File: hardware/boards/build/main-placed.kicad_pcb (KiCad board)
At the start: 4 copper layers, 177.9 x 107.5 mm, 146 parts

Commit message: Fix hardware pipeline: SD card position, faceplate holes, 3D assembly stack-up
- Fix SD card slot placement below PLAY button with component-map fallback
- Rebuild PJS008U 3D model as hollow card cage, align with faceplate cutout
- Inset USB-C connector flush with main board edge
- Add clock jack holes, SD cutout, JetBrains Mono fonts to faceplate
- Correct 3D assembly Z spacing from actual PJ398SM model measurements
- Improve explode animation: anchor control board, smoother slider
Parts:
- REF**: moved to F.Cu
- moved REF** 136.9 mm to (172.9, 53.8), turned to 90 degrees
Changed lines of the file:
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@@
 		)
 	)
+	(footprint "USB_C_Receptacle:USB_C_Receptacle"
+		(layer "F.Cu")
+		(at 172.88 53.75 90)
+		(property "Reference" "REF**"
+			(at 0 -6 90)
+			(layer "F.SilkS")
+			(effects
+				(font
+					(size 1 1)
+					(thickness 0.15)
+				)
+			)
+		)
+		(property "Value" "USB_C_Receptacle"
+			(at 0 6 90)
+			(layer "F.Fab")
+			(effects
+				(font
+					(size 1 1)
+					(thickness 0.15)
+				)
+			)
+		)
+		(property "Datasheet" ""
+			(at 0 0 90)
+			(layer "F.Fab")
+			(hide yes)
+			(effects
+				(font
+					(size 1.27 1.27)
+					(thickness 0.15)
+				)
+			)
+		)
+		(property "Description" ""
+			(at 0 0 90)
+			(layer "F.Fab")
+			(hide yes)
+			(effects
+				(font
+					(size 1.27 1.27)
+					(thickness 0.15)
+				)
+			)
+		)
+		(property "LCSC" "C165948"
+			(at 0 0 90)
+			(layer "User.9")
+			(hide yes)
+			(effects
+				(font
+					(size 1 1)
+					(thickness 0.15)
+				)
+			)
+		)
+		(property "Manufacturer" "Korean Hroparts Elec"
+			(at 0 0 90)
+			(layer "User.9")
+			(hide yes)
+			(effects
+				(font
+					(size 1 1)
+					(thickness 0.15)
+				)
+			)
+		)
+		(property "Partnumber" "TYPE-C-31-M-12"
+			(at 0 0 90)
+			(layer "User.9")
+			(hide yes)
+			(effects
+				(font
+					(size 1 1)
+					(thickness 0.15)
+				)
+			)
+		)
+		(property "atopile_address" "usb"
+			(at 0 0 90)
+			(layer "User.9")
+			(hide yes)
+			(effects
+				(font
+					(size 1 1)
+					(thickness 0.15)
+				)
+			)
+		)
+		(property "lcsc_id" "C165948"
+			(at 0 0 90)
+			(layer "User.9")
+			(hide yes)
+			(effects
+				(font
+					(size 1 1)
+					(thickness 0.15)
+				)
+			)
+		)
+		(attr smd)
+		(pad "" smd rect
+			(at -4.32 -1.45 90)
+			(size 1 2.1)
+			(layers "F.Cu" "F.Mask" "F.Paste")
+		)
+		(pad "1" smd rect
+			(at -3.2 -3.2 90)
+			(size 0.6 1.2)
+			(layers "F.Cu" "F.Mask" "F.Paste")
+			(net 34 "hv")
+		)
+		(pad "2" smd rect
+			(at -2.4 -3.2 90)
+			(size 0.6 1.2)
+			(layers "F.Cu" "F.Mask" "F.Paste")
+			(net 34 "hv")
+		)
+		(pad "3" smd rect
+			(at -0.8 -3.2 90)
+			(size 0.6 1.2)
+			(layers "F.Cu" "F.Mask" "F.Paste")
+			(net 142 "3")
+		)
+		(pad "4" smd rect
+			(at 0 -3.2 90)
+			(size 0.6 1.2)
+			(layers "F.Cu" "F.Mask" "F.Paste")
+			(net 145 "DM")
+		)
+		(pad "5" smd rect
+			(at 0.8 -3.2 90)
+			(size 0.6 1.2)
+			(layers "F.Cu" "F.Mask" "F.Paste")
+			(net 144 "5")
+		)
+		(pad "6" smd rect
+			(at 2.4 -3.2 90)
+			(size 0.6 1.2)
+			(layers "F.Cu" "F.Mask" "F.Paste")
+			(net 146 "6")
+		)
+		(pad "7" smd rect
+			(at 3.2 -3.2 90)
+			(size 0.6 1.2)
+			(layers "F.Cu" "F.Mask" "F.Paste")
+			(net 34 "hv")
+		)
+		(embedded_fonts no)
+		(model "${KICAD9_3DMODEL_DIR}/Connector_USB.3dshapes/USB_C_Receptacle_GCT_USB4085.step"
+			(offset (xyz -2.975 2.43 0))
+			(scale (xyz 1 1 1))
+			(rotate (xyz 0 0 0))
+		)
+	)
 	(footprint "ShroudedHeader2x16:ShroudedHeader2x16"
 		(layer "F.Cu")
@@
 		)
 	)
-	(footprint "USB_C_Receptacle:USB_C_Receptacle"
-		(layer "B.Cu")
-		(at 36 55.01 180)
-		(property "Reference" "REF**"
-			(at 0 6 0)
-			(layer "B.SilkS")
-			(effects
-				(font
-					(size 1 1)
-					(thickness 0.15)
-				)
-				(justify mirror)
-			)
-		)
-		(property "Value" "USB_C_Receptacle"
-			(at 0 -6 0)
-			(layer "B.Fab")
-			(effects
-				(font
-					(size 1 1)
-					(thickness 0.15)
-				)
-				(justify mirror)
-			)
-		)
-		(property "Datasheet" ""
-			(at 0 0 0)
-			(layer "B.Fab")
-			(hide yes)
-			(effects
-				(font
-					(size 1.27 1.27)
-					(thickness 0.15)
-				)
-				(justify mirror)
-			)
-		)
-		(property "Description" ""
-			(at 0 0 0)
-			(layer "B.Fab")
-			(hide yes)
-			(effects
-				(font
-					(size 1.27 1.27)
-					(thickness 0.15)
-				)
-				(justify mirror)
-			)
-		)
-		(property "LCSC" "C165948"
-			(at 0 0 0)
-			(layer "User.9")
-			(hide yes)
-			(effects
-				(font
-					(size 1 1)
-					(thickness 0.15)
-				)
-			)
-		)
-		(property "Manufacturer" "Korean Hroparts Elec"
-			(at 0 0 0)
-			(layer "User.9")
-			(hide yes)
-			(effects
-				(font
-					(size 1 1)
-					(thickness 0.15)
-				)
-			)
-		)
-		(property "Partnumber" "TYPE-C-31-M-12"
-			(at 0 0 0)
-			(layer "User.9")
-			(hide yes)
-			(effects
-				(font
-					(size 1 1)
-					(thickness 0.15)
-				)
-			)
-		)
-		(property "atopile_address" "usb"
-			(at 0 0 0)
-			(layer "User.9")
-			(hide yes)
-			(effects
-				(font
-					(size 1 1)
-					(thickness 0.15)
-				)
-			)
-		)
-		(property "lcsc_id" "C165948"
-			(at 0 0 0)
-			(layer "User.9")
-			(hide yes)
-			(effects
-				(font
-					(size 1 1)
-					(thickness 0.15)
-				)
-			)
-		)
-		(attr smd)
-		(pad "" smd rect
-			(at -4.32 1.45 180)
-			(size 1 2.1)
-			(layers "B.Cu" "B.Mask" "B.Paste")
-		)
-		(pad "1" smd rect
-			(at -3.2 3.2 180)
-			(size 0.6 1.2)
-			(layers "B.Cu" "B.Mask" "B.Paste")
-			(net 34 "hv")
-		)
-		(pad "2" smd rect
-			(at -2.4 3.2 180)
-			(size 0.6 1.2)
-			(layers "B.Cu" "B.Mask" "B.Paste")
-			(net 34 "hv")
-		)
-		(pad "3" smd rect
-			(at -0.8 3.2 180)
-			(size 0.6 1.2)
-			(layers "B.Cu" "B.Mask" "B.Paste")
-			(net 142 "3")
-		)
-		(pad "4" smd rect
-			(at 0 3.2 180)
-			(size 0.6 1.2)
-			(layers "B.Cu" "B.Mask" "B.Paste")
-			(net 145 "DM")
-		)
-		(pad "5" smd rect
-			(at 0.8 3.2 180)
-			(size 0.6 1.2)
-			(layers "B.Cu" "B.Mask" "B.Paste")
-			(net 144 "5")
-		)
-		(pad "6" smd rect
-			(at 2.4 3.2 180)
-			(size 0.6 1.2)
-			(layers "B.Cu" "B.Mask" "B.Paste")
-			(net 146 "6")
-		)
-		(pad "7" smd rect
-			(at 3.2 3.2 180)
-			(size 0.6 1.2)
-			(layers "B.Cu" "B.Mask" "B.Paste")
-			(net 34 "hv")
-		)
-		(embedded_fonts no)
-		(model "${KICAD9_3DMODEL_DIR}/Connector_USB.3dshapes/USB_C_Receptacle_GCT_USB4085.step"
-			(offset (xyz -2.975 2.43 0))
-			(scale (xyz 1 1 1))
-			(rotate (xyz 0 0 0))
-		)
-	)
 	(footprint "AMS1117-3.3:SOT-223"
 		(layer "B.Cu")
@@
 	)
 	(gr_line
-		(start 0 0)
-		(end 177.88 0)
+		(start 177.88 0)
+		(end 177.88 107.5)
 		(stroke
 			(width 0.1)
@@
 	)
 	(gr_line
-		(start 0 107.5)
-		(end 0 0)
+		(start 0 0)
+		(end 177.88 0)
 		(stroke
 			(width 0.1)
@@
 	)
 	(gr_line
-		(start 177.88 107.5)
-		(end 0 107.5)
+		(start 0 107.5)
+		(end 0 0)
 		(stroke
 			(width 0.1)
@@
 	)
 	(gr_line
-		(start 177.88 0)
-		(end 177.88 107.5)
+		(start 177.88 107.5)
+		(end 0 107.5)
 		(stroke
 			(width 0.1)

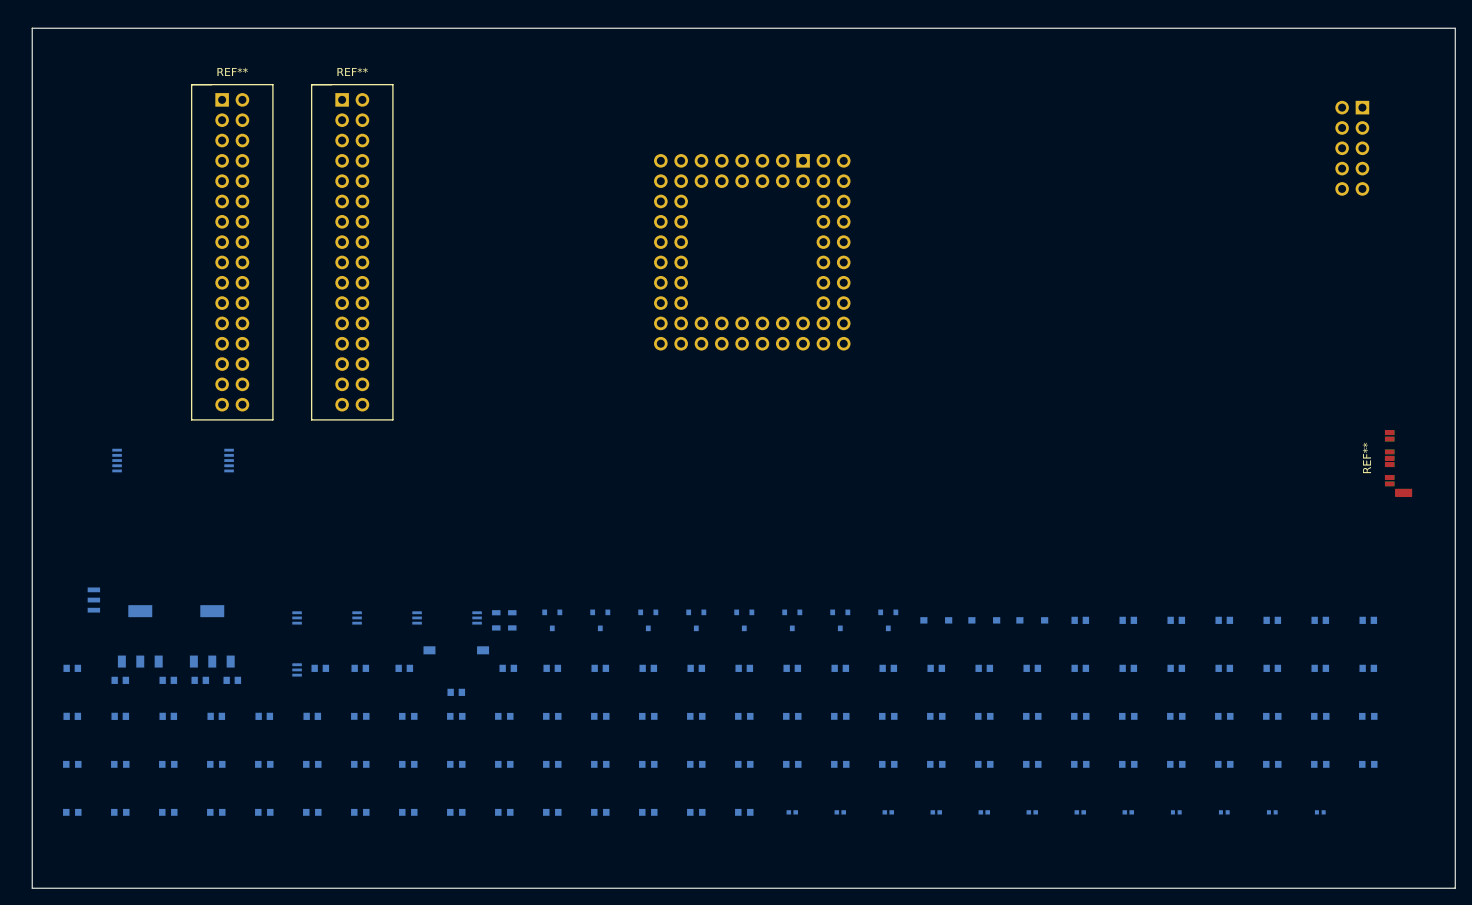
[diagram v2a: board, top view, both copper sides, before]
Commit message: Routing with design-rules.json
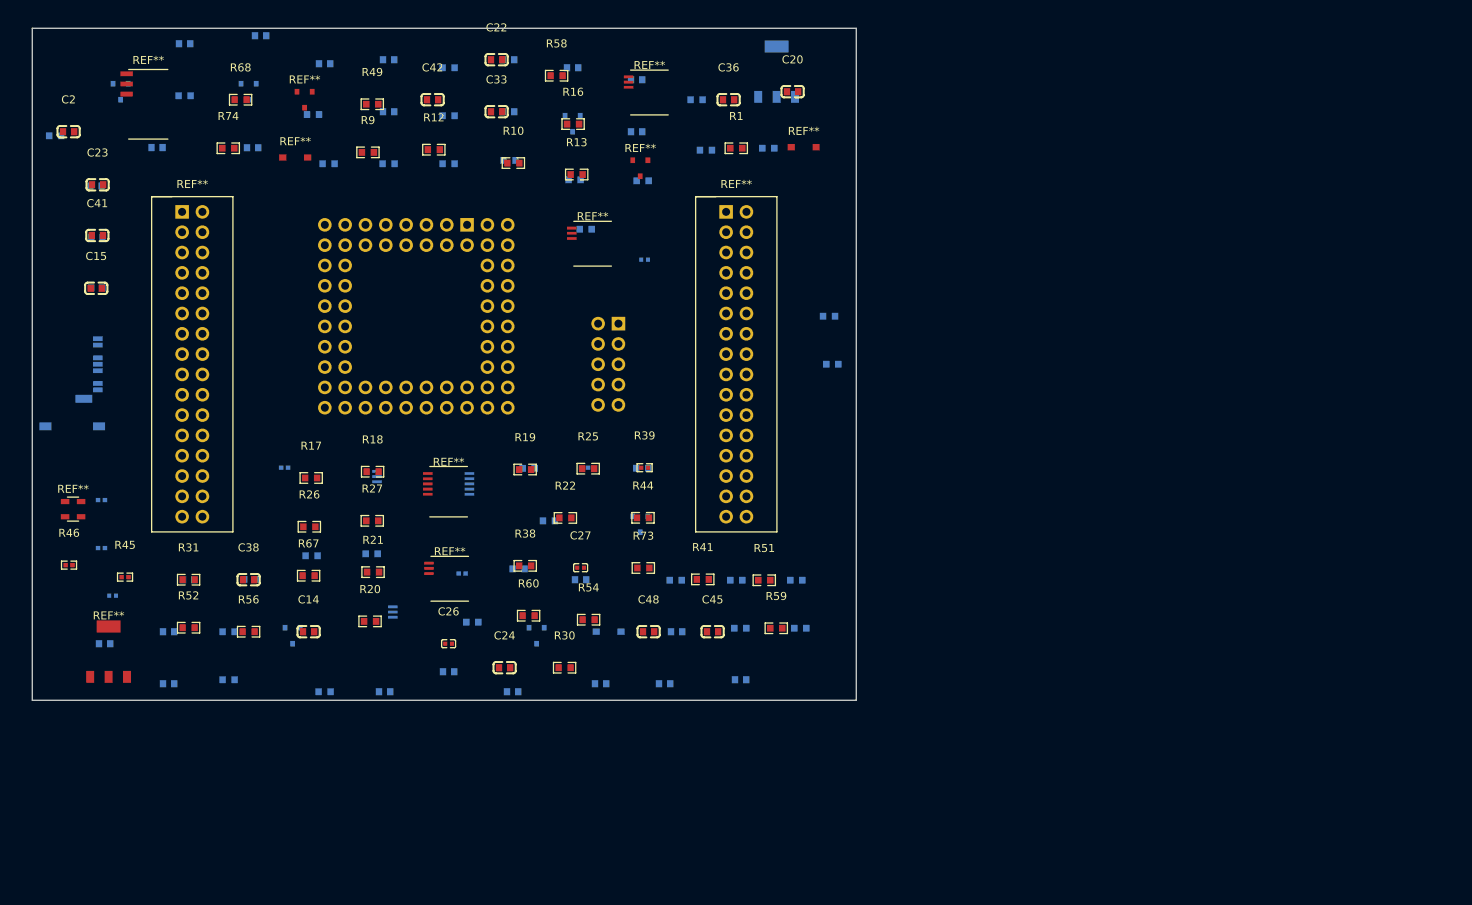
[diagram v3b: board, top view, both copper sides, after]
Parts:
- C14, C15, C2, C20, C22, C23, C24, C26, C27, C33, C36, C38, C41, C42, C45, C48, R1, R10, R12, R13, R16, R17, R18, R19, R20, R21, R22, R25, R26, R27, R30, R31, R38, R39, R41, R44, R45, R46, R49, R51, R52, R54, R56, R58, R59, R60, R67, R68, R73, R74, R9, REF** (x11): moved to F.Cu
- REF**: moved to B.Cu
- moved REF** 168.3 mm to (5.00, 42.0)
- moved C41 156.5 mm to (8.13, 25.9), turned to 0 degrees
- moved C8 153.4 mm to (7.98, 19.7)
- moved C23 147.8 mm to (8.17, 19.6), turned to 0 degrees
- moved C25 141.6 mm to (10.0, 70.9)
- moved C31 141.1 mm to (44.5, 3.93)
- moved C34 140.8 mm to (44.5, 10.4)
- moved C21 137.4 mm to (8.07, 32.4)
- moved R69 136.9 mm to (24.5, 75.4)
- moved R46 136.0 mm to (4.60, 67.1), turned to 0 degrees
- moved R66 134.8 mm to (52.0, 4.93)
- moved C38 134.1 mm to (27.0, 68.9), turned to 0 degrees
- moved C19 128.7 mm to (8.08, 26.1)
- moved R50 127.4 mm to (52.0, 10.9)
- moved R48 126.9 mm to (2.86, 13.4)
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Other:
- board size 177.9 x 107.5 mm -> 103 x 84 mm

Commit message: Refactor hardware pipeline: config-driven scripts, immutable build stages, full 3D export
- Reorganize scripts/ into build/, common/, placement/, routing/, export/, models/
- Replace autoroute.sh (389 lines bash) with autoroute.py (pure Python)
- Extract board-specific values into board-config.json (placement, routing, DRC allowlist)
- Create hardware/Makefile with file-based dependencies covering full pipeline
- Immutable pipeline: placed → routed → poured → 3d → step → glb (no in-place mutation)
- Ground pours now read clearances from design-rules.json
- DRC allowlisting for known SD card footprint errors
- 3D pipeline: add_3d_models → export_3d_assembly (STEP) → export_gltf (GLB with named nodes)
- Simplify root Makefile to delegate hw-* targets to hardware/Makefile
- Remove Docker/CI workflows (unused), old flat scripts, pycache
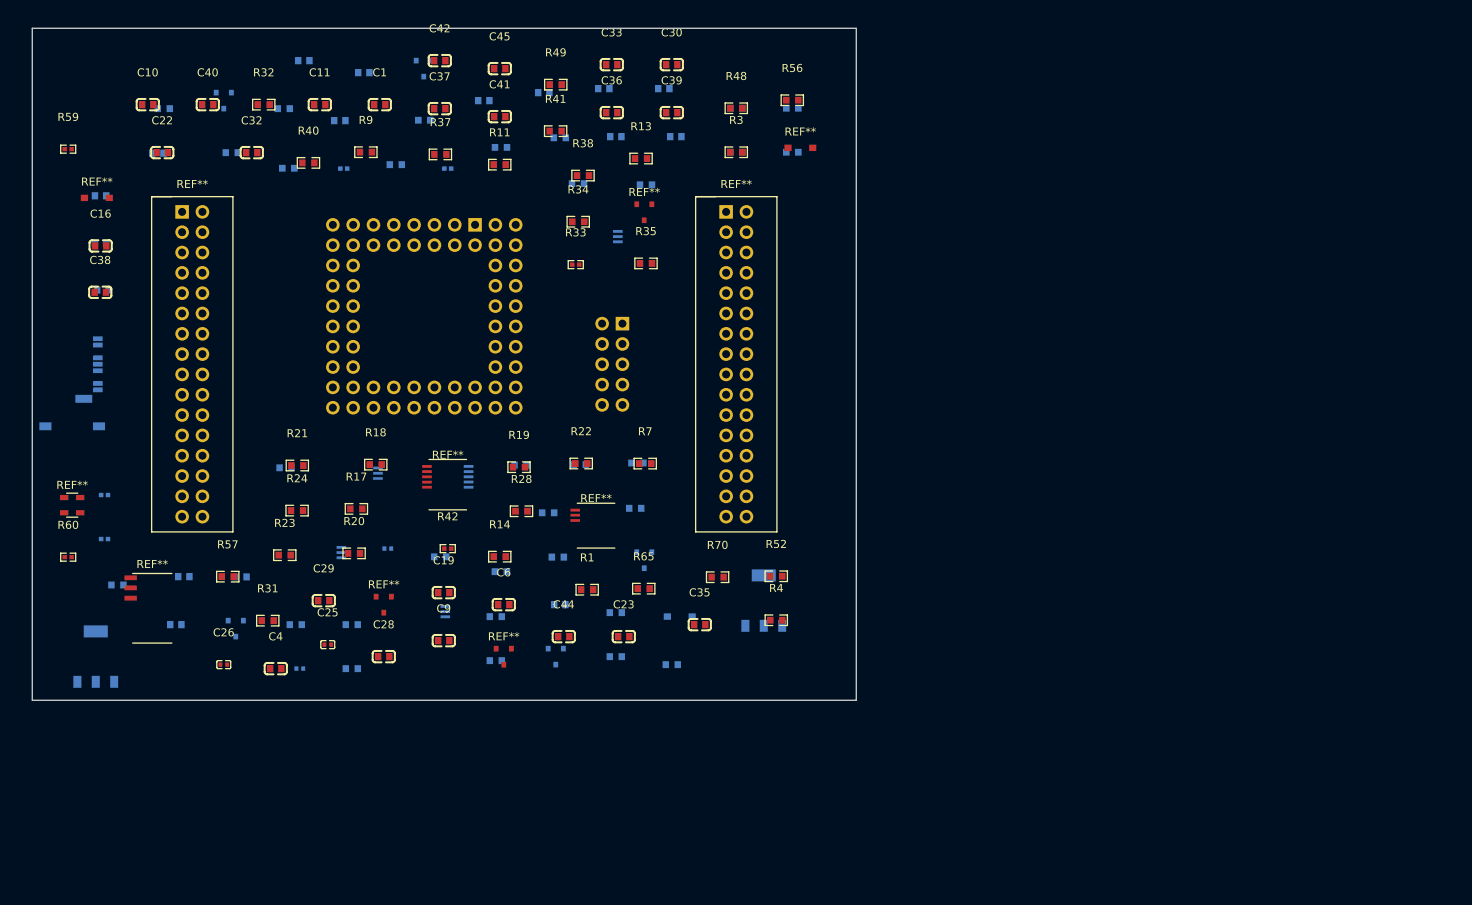
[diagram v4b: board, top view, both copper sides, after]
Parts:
- removed C46, C47, C48: 0F, YAGEO_CC0603KRX7R9BB104:C0603
- removed R74: 10000Ω, UNI_ROYAL_0603WAF1002T5E:R0603
- removed R75, R76: 27Ω, UNI_ROYAL_0402WGF270JTCE:R0402
- removed the REF** at (76.0, 17.5)
- removed the REF** at (70.0, 26.9)
- removed the REF** at (32.9, 16.2)
- removed the REF** at (77.1, 8.03)
- removed the REF** at (11.0, 7.93)
- removed the REF** at (72.0, 75.4)
- removed the REF** at (76.0, 62.0)
- removed the REF** at (67.5, 11.9)
- removed the REF** at (42.5, 74.3)
- removed the REF** at (52.2, 68.8)
- removed the REF** at (63.0, 75.9)
- removed the REF** at (40.5, 57.3)
- removed the REF** at (27.0, 7.93)
- removed the REF** at (52.0, 57.9) (x2)
- removed the REF** at (32.5, 75.9)
- removed the REF** at (34.0, 8.93)
- removed the REF** at (96.4, 14.9)
- added C29: 0F, YAGEO_CC0603KRX7R9BB104:C0603, F.Cu at (36.4, 71.5)
- added C30: 0F, YAGEO_CC0603KRX7R9BB104:C0603, F.Cu at (79.9, 4.55)
- added C7: 0F, Samsung_Electro_Mechanics_CL10A106KP8NNNC:C0603, B.Cu at (8.82, 32.7)
- added R47: 10000Ω, UNI_ROYAL_0603WAF1002T5E:R0603, B.Cu at (32.9, 74.5)
- added R62: 1000Ω, UNI_ROYAL_0603WAF1001T5E:R0603, B.Cu at (76.7, 19.6)
- added R63: 10000Ω, UNI_ROYAL_0603WAF1002T5E:R0603, B.Cu at (24.9, 15.5)
- added REF**: SOT-23, BAT54S:SOT-23, F.Cu at (58.9, 78.5)
- added REF**: SOT-23, 2N3904:SOT-23, F.Cu at (76.5, 23.0)
- added REF**: SOT-23, BAT54S:SOT-23, B.Cu at (23.9, 9.05)
- added REF**: TSSOP-16, DAC8568SPMR:TSSOP-16, B.Cu at (51.9, 57.0)
- added REF**: SOT-23, BAT54S:SOT-23, B.Cu at (48.9, 5.05)
- added REF**: SOD-123, B5819W:SOD-123, F.Cu at (96.0, 14.9)
- added REF**: SOD-123, B5819W:SOD-123, B.Cu at (80.9, 73.5)
- added REF**: TSSOP-14, OPA4172ID:TSSOP-14, B.Cu at (49.0, 74.2)
- added REF**: SOT-23, BAT54S:SOT-23, B.Cu at (25.4, 75.0)
- added REF**: SOT-23, 2N3904:SOT-23, B.Cu at (76.5, 66.5)
- added REF**: TSSOP-14, OPA4172ID:TSSOP-14, B.Cu at (40.6, 56.9)
- added REF**: TSSOP-14, OPA4172ID:TSSOP-14, B.Cu at (70.6, 27.3)
- added REF**: TSSOP-14, OPA4172ID:TSSOP-14, B.Cu at (36.0, 66.8)
- added REF**: SOT-23, BAT54S:SOT-23, B.Cu at (65.4, 78.5)
- added REF**: TSSOP-16, DAC8568SPMR:TSSOP-16, F.Cu at (51.9, 57.0)
- added REF**: SOD-123, B5819W:SOD-123, F.Cu at (8.07, 21.2)
- added REF**: TSSOP-14, OPA4172ID:TSSOP-14, F.Cu at (70.5, 62.2)
- added REF**: SOT-23, BAT54S:SOT-23, F.Cu at (43.9, 72.0)
- C1, C16, C19, C25, C32, C35, C37, C4, C44, C6, R11, R14, R23, R24, R28, R3, R32, R33, R34, R35, R37, R4, R40, R42, R7: moved to F.Cu
- C10, C39: footprint YAGEO_CC0603KRX7R9BB104:C0603 -> Samsung_Electro_Mechanics_CL10A106KP8NNNC:C0603; moved to F.Cu
- C11, C40, C9: footprint Samsung_Electro_Mechanics_CL10A106KP8NNNC:C0603 -> YAGEO_CC0603KRX7R9BB104:C0603; moved to F.Cu
- C12, C38: footprint YAGEO_CC0603KRX7R9BB104:C0603 -> Samsung_Electro_Mechanics_CL10A106KP8NNNC:C0603
- C13, C41, C42: footprint Samsung_Electro_Mechanics_CL10A106KP8NNNC:C0603 -> YAGEO_CC0603KRX7R9BB104:C0603
- C14, C15, C2, C20, C27, R10, R12, R16, R25, R26, R27, R30, R39, R44, R67, R68, REF**: moved to B.Cu
- C24: footprint YAGEO_CC0603KRX7R9BB104:C0603 -> Samsung_Electro_Mechanics_CL05A105KA5NQNC:C0402; moved to B.Cu
- C28: footprint Samsung_Electro_Mechanics_CL05A105KA5NQNC:C0402 -> Samsung_Electro_Mechanics_CL10A106KP8NNNC:C0603; moved to F.Cu
- R45, R46: value 5100Ω -> 10000Ω; footprint UNI_ROYAL_0402WGF5101TCE:R0402 -> UNI_ROYAL_0603WAF1002T5E:R0603; moved to B.Cu
- R48: value 10000Ω -> 22000Ω; footprint UNI_ROYAL_0603WAF1002T5E:R0603 -> UNI_ROYAL_0603WAF2202T5E:R0603; moved to F.Cu
- R50, R52, R56: value 10000Ω -> 22000Ω; footprint UNI_ROYAL_0603WAF1002T5E:R0603 -> UNI_ROYAL_0603WAF2202T5E:R0603
- R51: value 22000Ω -> 10000Ω; footprint UNI_ROYAL_0603WAF2202T5E:R0603 -> UNI_ROYAL_0603WAF1002T5E:R0603; moved to B.Cu
- R53, R55: value 22000Ω -> 10000Ω; footprint UNI_ROYAL_0603WAF2202T5E:R0603 -> UNI_ROYAL_0603WAF1002T5E:R0603
- R54, R58: value 10000Ω -> 22000Ω; footprint UNI_ROYAL_0603WAF1002T5E:R0603 -> UNI_ROYAL_0603WAF2202T5E:R0603; moved to B.Cu
- R57: value 22000Ω -> 10000Ω; footprint UNI_ROYAL_0603WAF2202T5E:R0603 -> UNI_ROYAL_0603WAF1002T5E:R0603; moved to F.Cu
- R59: value 22000Ω -> 5100Ω; footprint UNI_ROYAL_0603WAF2202T5E:R0603 -> UNI_ROYAL_0402WGF5101TCE:R0402
- R60: value 10000Ω -> 5100Ω; footprint UNI_ROYAL_0603WAF1002T5E:R0603 -> UNI_ROYAL_0402WGF5101TCE:R0402
- R61: value 22000Ω -> 1000Ω; footprint UNI_ROYAL_0603WAF2202T5E:R0603 -> UNI_ROYAL_0603WAF1001T5E:R0603
- R64: value 1000Ω -> 10000Ω; footprint UNI_ROYAL_0603WAF1001T5E:R0603 -> UNI_ROYAL_0603WAF1002T5E:R0603
- R65: value 1000Ω -> 10000Ω; footprint UNI_ROYAL_0603WAF1001T5E:R0603 -> UNI_ROYAL_0603WAF1002T5E:R0603; moved to F.Cu
- R69: value 10000Ω -> 1000Ω; footprint UNI_ROYAL_0603WAF1002T5E:R0603 -> UNI_ROYAL_0603WAF1001T5E:R0603
- R70: value 10000Ω -> 1000Ω; footprint UNI_ROYAL_0603WAF1002T5E:R0603 -> UNI_ROYAL_0603WAF1001T5E:R0603; moved to F.Cu
- R72: value 1000Ω -> 27Ω; footprint UNI_ROYAL_0603WAF1001T5E:R0603 -> UNI_ROYAL_0402WGF270JTCE:R0402
- R73: value 1000Ω -> 27Ω; footprint UNI_ROYAL_0603WAF1001T5E:R0603 -> UNI_ROYAL_0402WGF270JTCE:R0402; moved to B.Cu
- moved R59 106.9 mm to (4.49, 15.1)
- moved R56 95.0 mm to (95.0, 9.00)
- moved C10 91.9 mm to (14.4, 9.55), turned to 0 degrees
- moved C11 89.1 mm to (35.9, 9.55), turned to 0 degrees
- moved C44 88.0 mm to (66.4, 76.0), turned to 0 degrees
- moved C20 87.5 mm to (8.54, 20.9), turned to 180 degrees
- moved C23 86.7 mm to (73.9, 76.0)
- moved R30 86.0 mm to (16.4, 10.0), turned to 180 degrees
- moved R48 85.2 mm to (88.0, 10.0), turned to 0 degrees
- moved C13 84.4 mm to (17.9, 74.5)
- moved C32 84.1 mm to (27.4, 15.5), turned to 0 degrees
- moved C35 81.7 mm to (83.4, 74.5), turned to 0 degrees
- moved R66 79.7 mm to (79.9, 79.5)
- moved C40 77.0 mm to (21.9, 9.55), turned to 0 degrees
- moved C45 75.2 mm to (58.4, 5.05)
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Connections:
- C14 pad 1: c_lvl-power-hv -> hv
- C14 pad 2: hv -> lv
- C15 pad 1: hv -> c_op5_p-power-hv
- C15 pad 2: lv -> hv
- C16 pad 1: c_op5_p-power-hv -> hv
- C16 pad 2: hv -> lv
- C17 pad 1: hv -> c_op5_p-power-hv
- C17 pad 2: lv -> hv
- C18 pad 1: c_op5_p-power-hv -> hv
- C18 pad 2: hv -> lv
- C19 pad 1: hv -> c_op5_p-power-hv
- C19 pad 2: lv -> hv
- C20 pad 1: c_op5_p-power-hv -> hv
- C20 pad 2: hv -> lv
- C21 pad 1: hv -> c_op5_p-power-hv
- C21 pad 2: lv -> hv
- C22 pad 1: c_op5_p-power-hv -> hv
- C22 pad 2: hv -> lv
- C23 pad 1: hv -> c_op5_p-power-hv
- C23 pad 2: lv -> hv
- C24 pad 1: c_op5_p-power-hv -> c_pitch_ref-power-hv
- C25 pad 1: c_pitch_ref-power-hv -> c_ref1-power-hv
- C26 pad 1: c_ref1-power-hv -> c_ref2-power-hv
- C27 pad 1: c_ref2-power-hv -> c_ref_filt-power-hv
- C28 pad 1: c_ref_filt-power-hv -> c_3v3_bulk-power-hv
- C31 pad 1: c_3v3_bulk-power-hv -> c_vb-power-hv
- C32 pad 1: c_3v3_bulk-power-hv -> c_lvl-power-hv
- C33 pad 1: c_aref-power-hv -> c_3v3_out_hf-power-hv
- C34 pad 1: c_vb-power-hv -> c_3v3_out_hf-power-hv
- C35 pad 1: c_lvl-power-hv -> c_op5_p-power-hv
- C36 pad 1: c_3v3_out_hf-power-hv -> c_lvl-power-hv
- C37 pad 1: c_3v3_out_hf-power-hv -> c_lvl-power-hv
- C38 pad 1: c_op5_p-power-hv -> hv
- C38 pad 2: hv -> lv
- C39 pad 1: c_lvl-power-hv -> c_op5_p-power-hv
- C40 pad 1: c_lvl-power-hv -> c_filter-power-hv
- C41 pad 1: hv -> c_filter-power-hv-1
- C41 pad 2: lv -> hv
- C42 pad 1: c_op5_p-power-hv -> c_filter-power-hv-2
- C43 pad 1: c_filter-power-hv -> c_filter-power-hv-3
- C44 pad 1: c_filter-power-hv-1 -> c_filter-power-hv-4
- C45 pad 1: c_filter-power-hv-2 -> c_filter-power-hv-5
- C8 pad 1: hv -> c_op5_p-power-hv
- C8 pad 2: lv -> hv
- C9 pad 1: c_op5_p-power-hv -> c_lvl-power-hv
- R45 pad 1: 5 -> c_3v3_bulk-power-hv
- R45 pad 2: hv -> BS
- R46 pad 1: 6 -> c_3v3_bulk-power-hv
- R46 pad 2: hv -> RUN
- R48 pad 1: c_3v3_bulk-power-hv -> clk_in
- R48 pad 2: BS -> c_filter-power-hv
- R49 pad 1: c_3v3_bulk-power-hv -> c_filter-power-hv-1
- R49 pad 2: RUN -> hv
- R50 pad 1: c_filter-power-hv -> cv_a
- R50 pad 2: hv -> c_filter-power-hv-1
- R51 pad 1: clk_in -> c_filter-power-hv-2
- R51 pad 2: c_filter-power-hv -> hv
- R52 pad 1: c_filter-power-hv-1 -> cv_b
- R52 pad 2: hv -> c_filter-power-hv-2
- R53 pad 1: cv_a -> c_filter-power-hv-3
- R53 pad 2: c_filter-power-hv-1 -> hv
- R54 pad 1: c_filter-power-hv-2 -> cv_c
- R54 pad 2: hv -> c_filter-power-hv-3
- R55 pad 1: cv_b -> c_filter-power-hv-4
- R55 pad 2: c_filter-power-hv-2 -> hv
- R56 pad 1: c_filter-power-hv-3 -> cv_d
- R56 pad 2: hv -> c_filter-power-hv-4
- R57 pad 1: cv_c -> c_filter-power-hv-5
- R57 pad 2: c_filter-power-hv-3 -> hv
- R58 pad 1: c_filter-power-hv-4 -> input
- R58 pad 2: hv -> c_filter-power-hv-5
- R59 pad 1: cv_d -> 5
- R59 pad 2: c_filter-power-hv-4 -> hv
- R60 pad 1: c_filter-power-hv-5 -> 6
- R61 pad 1: input -> clk_out
- R61 pad 2: c_filter-power-hv-5 -> BASE
- R64 pad 1: clk_out -> c_3v3_out_hf-power-hv
- R64 pad 2: BASE -> c_enc_a_b-power-hv
- R65 pad 1: c_lvl-power-hv -> c_3v3_out_hf-power-hv
- R65 pad 2: COLLECTOR -> c_enc_a_sw-power-hv
- R66 pad 2: c_enc_a_a-power-hv -> c_enc_b_a-power-hv
- R67 pad 2: c_enc_a_b-power-hv -> c_enc_b_b-power-hv
- R68 pad 2: c_enc_a_sw-power-hv -> c_enc_b_sw-power-hv
- R69 pad 1: c_3v3_out_hf-power-hv -> rst_out
- R69 pad 2: c_enc_b_a-power-hv -> BASE-1
- R70 pad 1: c_3v3_out_hf-power-hv -> c_lvl-power-hv
- R70 pad 2: c_enc_b_b-power-hv -> COLLECTOR-1
- R71 pad 2: c_enc_b_sw-power-hv -> sd_cd
- R72 pad 1: rst_out -> usb_dm
- R72 pad 2: BASE-1 -> DM
- R73 pad 1: c_lvl-power-hv -> usb_dp
- R73 pad 2: COLLECTOR-1 -> 3
